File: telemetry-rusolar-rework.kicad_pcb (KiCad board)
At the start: 2 copper layers, 131 parts, among them IC1 TLV62569DBVR, J1 USART Debug, J10 JP, J12 I2C, J13 GR2, J14 GR1, J15 N_GR1, J19 Micro_SD_Card, J2 SPI, J20 USB_C_Receptacle_USB2.0_14P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

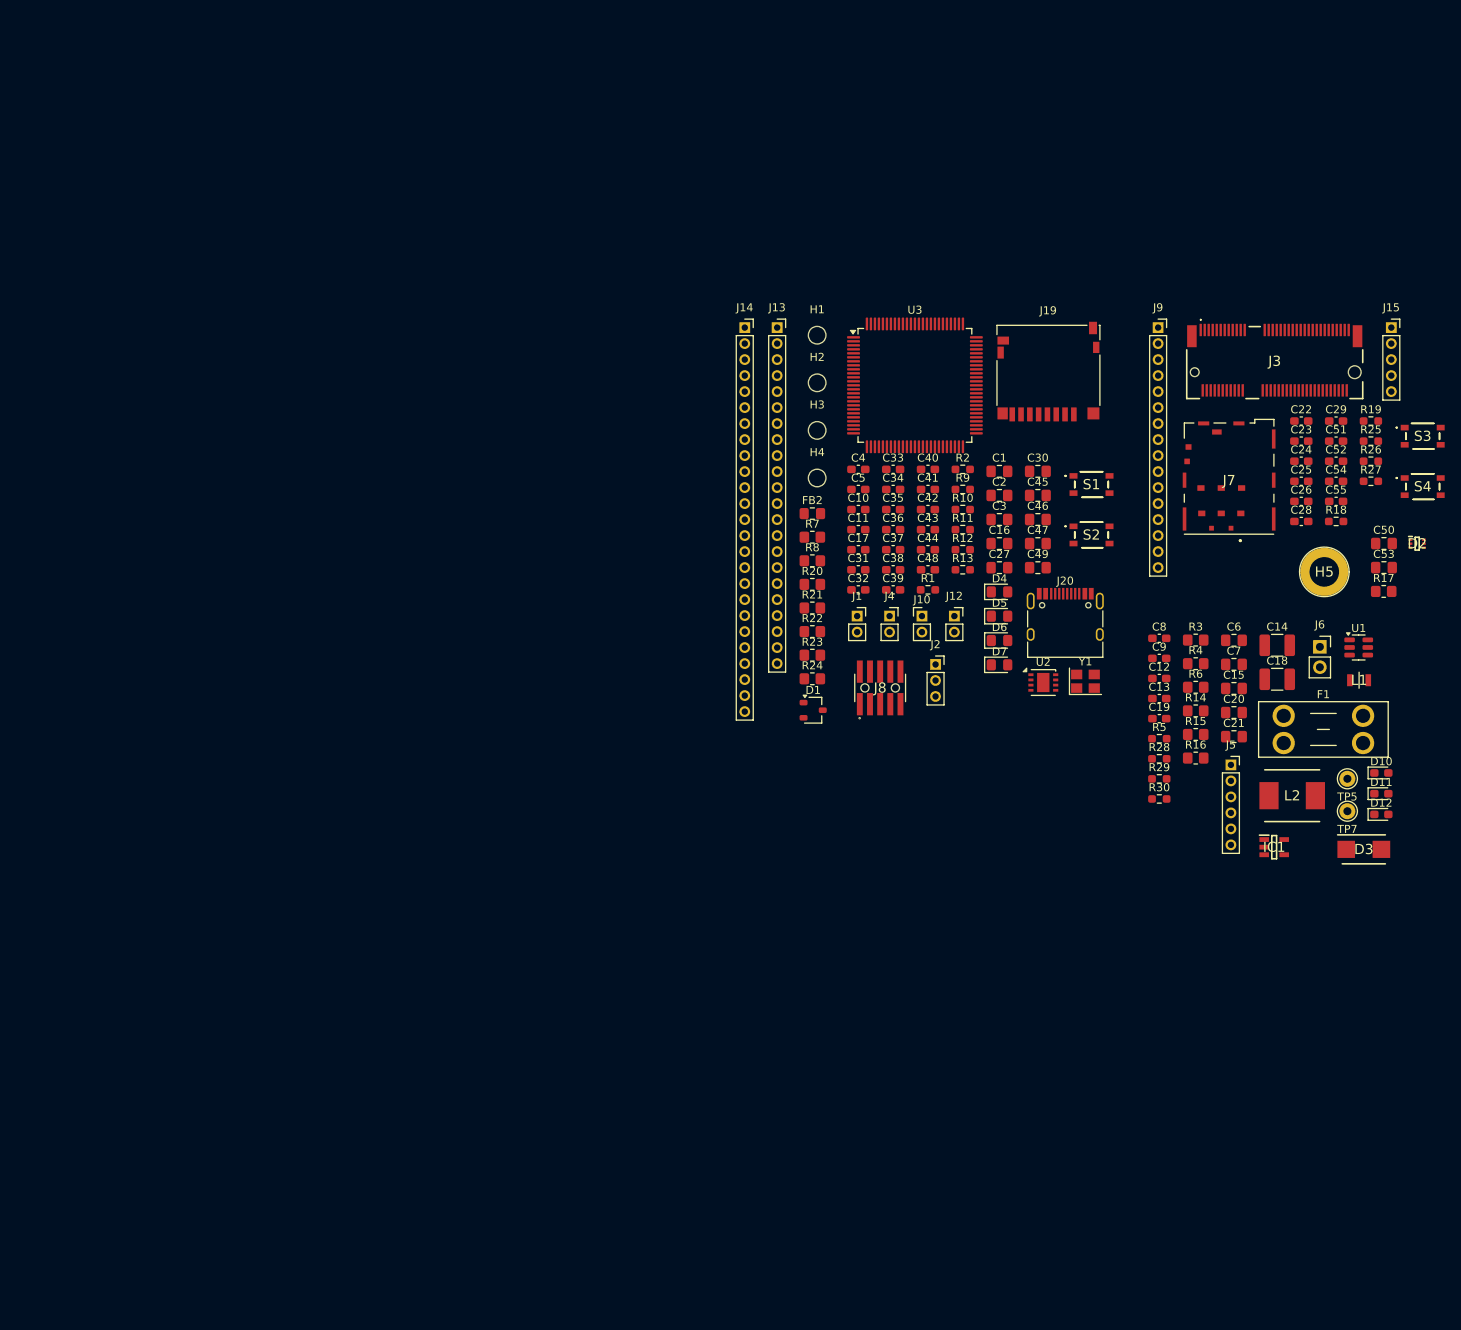
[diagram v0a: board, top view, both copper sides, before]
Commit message: Layout parts
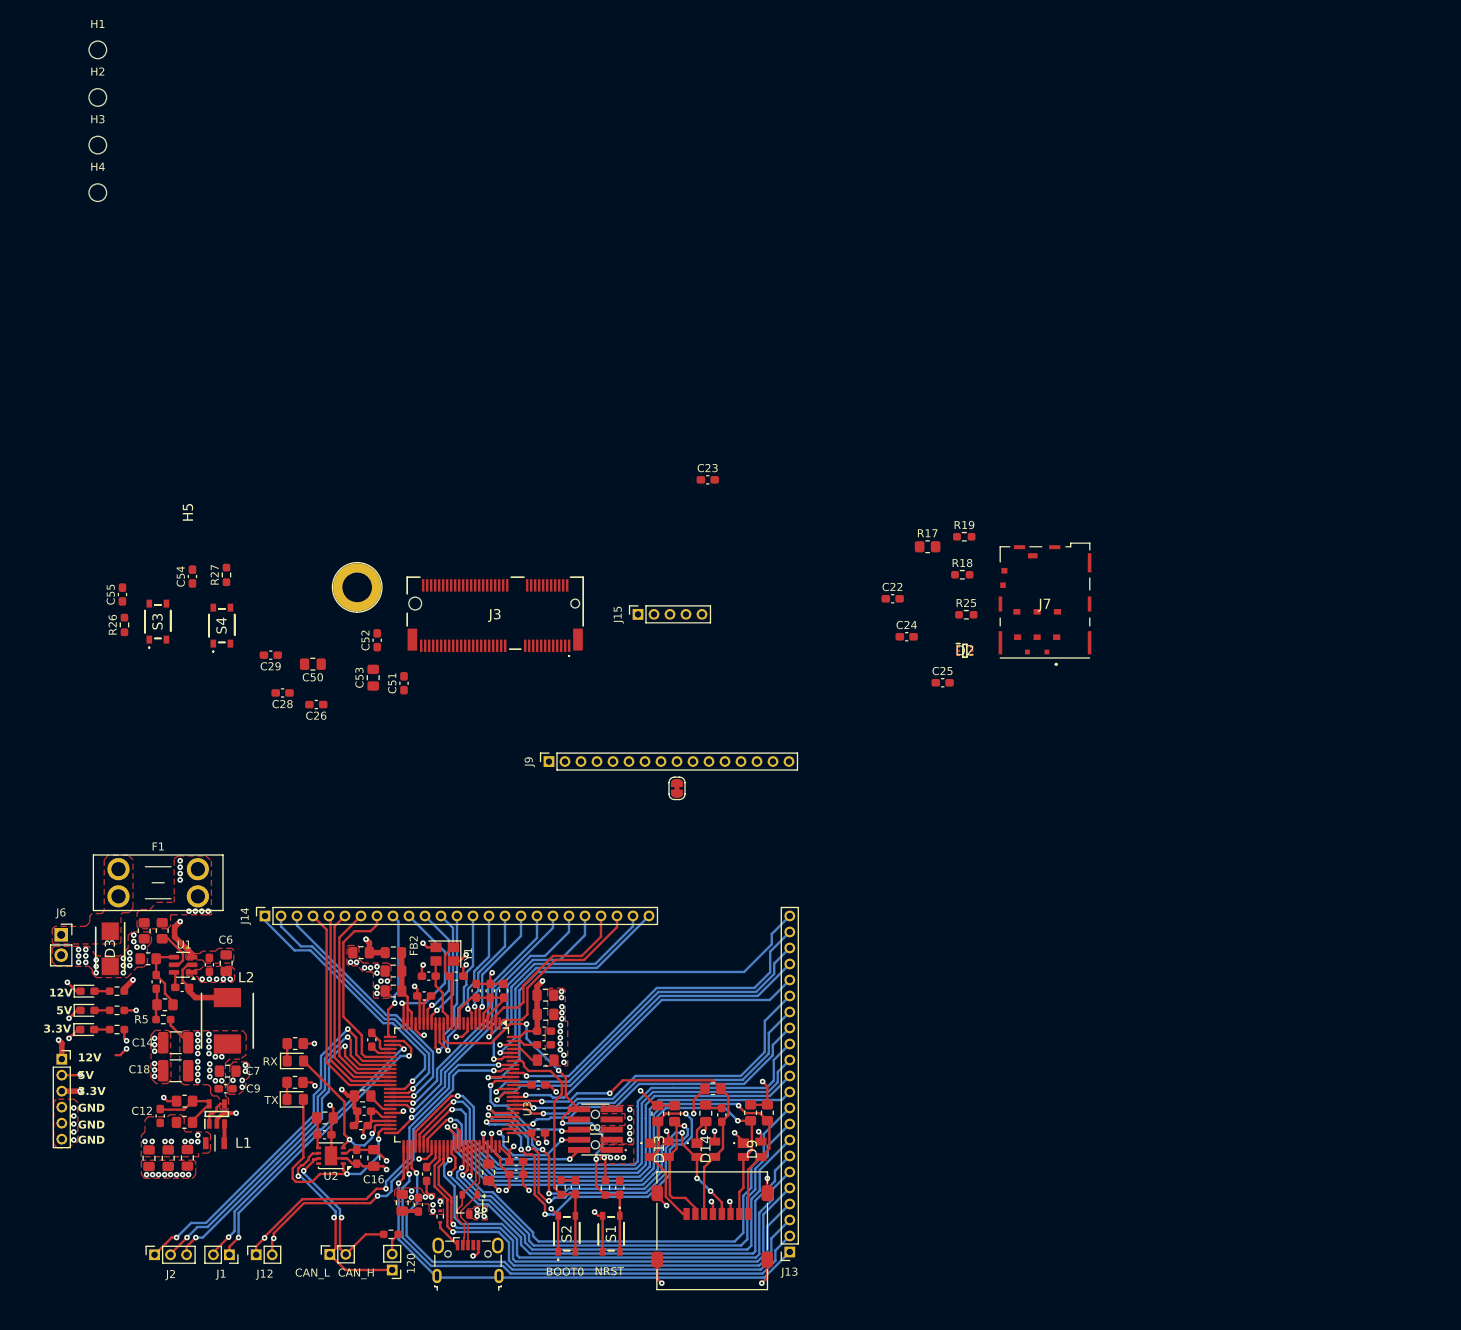
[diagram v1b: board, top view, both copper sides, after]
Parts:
- removed D4: SD-ON, LED_SMD:LED_0805_2012Metric_Pad1.15x1.40mm_HandSolder
- removed D7: PWR, LED_SMD:LED_0805_2012Metric_Pad1.15x1.40mm_HandSolder
- removed J20: USB_C_Receptacle_USB2.0_14P, Connector_USB:USB_C_Receptacle_HRO_TYPE-C-31-M-12
- removed R10, R11: 5k1, Resistor_SMD:R_0603_1608Metric_Pad0.98x0.95mm_HandSolder
- removed R12: 1k5, Resistor_SMD:R_0603_1608Metric_Pad0.98x0.95mm_HandSolder
- removed R9: 330, Resistor_SMD:R_0603_1608Metric_Pad0.98x0.95mm_HandSolder
- removed TP5, TP7: OUT_TP, Connector_Pin:Pin_D1.0mm_L10.0mm
- added C56: 100n, Capacitor_SMD:C_0603_1608Metric_Pad1.08x0.95mm_HandSolder, F.Cu at (70.3, 166.5)
- added C57: 1u, Capacitor_SMD:C_0805_2012Metric_Pad1.18x1.45mm_HandSolder, F.Cu at (68.2, 166.2)
- added C58: 100n, Capacitor_SMD:C_0603_1608Metric_Pad1.08x0.95mm_HandSolder, F.Cu at (58.5, 157.8)
- added C59: 10u, Capacitor_SMD:C_0805_2012Metric_Pad1.18x1.45mm_HandSolder, F.Cu at (58.6, 155.7)
- added D13: LSR05-TP, SamacSys_Parts:LSR05TP, F.Cu at (100.4, 159.6)
- added D14: LSR05-TP, SamacSys_Parts:LSR05TP, F.Cu at (106.2, 159.6)
- added D8: VESD05A1-02VHG3-08, SamacSys_Parts:VESD05A102VHG308, F.Cu at (73.0, 168.0)
- added D9: LSR05-TP, SamacSys_Parts:LSR05TP, F.Cu at (112.0, 159.6)
- added J11: USB_B_Micro, Connector_USB:USB_Micro-B_Wuerth_629105150521, F.Cu at (76.5, 173.4)
- added JP1: SolderJumper, Jumper:SolderJumper-2_P1.3mm_Bridged_RoundedPad1.0x1.5mm, F.Cu at (102.6, 114.5)
- J19: footprint Connector_Card:microSD_HC_Hirose_DM3D-SF -> Connector_Card:microSD_HC_Molex_47219-2001
- moved D10 164.0 mm to (28.9, 139.8)
- moved D12 164.0 mm to (28.9, 144.6)
- moved D11 164.0 mm to (28.9, 142.2)
- moved J6 161.4 mm to (25.6, 132.8)
- moved S3 159.8 mm to (37.7, 93.6), turned to 90 degrees
- moved D3 157.2 mm to (31.8, 134.5), turned to -90 degrees
- moved R26 157.1 mm to (33.5, 94.0), turned to 90 degrees
- moved L1 154.3 mm to (44.9, 158.8), turned to 180 degrees
- moved U1 152.2 mm to (40.9, 136.5), turned to 180 degrees
- moved C55 152.2 mm to (33.3, 90.2), turned to 90 degrees
- moved S4 151.1 mm to (45.7, 94.1), turned to 90 degrees
- moved J5 150.7 mm to (25.7, 148.3)
- moved C15 147.8 mm to (36.6, 160.7), turned to -90 degrees
- moved C14 146.4 mm to (39.9, 146.2), turned to 180 degrees
- moved C18 146.1 mm to (39.9, 149.8), turned to 180 degrees
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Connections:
- C2 pad 2: Net-(C1-Pad2) -> Net-(C2-Pad2)
- C3 pad 2: Net-(C1-Pad2) -> Net-(C3-Pad2)
- D1 pad 1: /USB_D- -> /USB_D+
- D1 pad 2: /USB_D+ -> /USB_D-
- J10 pad 1: /CAN2_RX -> /CAN_N
- J13 pad 1: /PA0 -> /PB15
- J13 pad 10: /PB2 -> /PA10
- J13 pad 11: /PB4 -> /PD13
- J13 pad 12: /PB5 -> /PD12
- J13 pad 13: /PB8 -> /PD11
- J13 pad 14: /PB9 -> /PD10
- J13 pad 15: /PB10 -> /PA15
- J13 pad 16: /PB11 -> /PD0
- J13 pad 17: /PB14 -> /PD1
- J13 pad 18: /PB15 -> /PD3
- J13 pad 19: /PC0 -> /PD4
- J13 pad 2: /PA1 -> /PD8
- J13 pad 20: /PC1 -> /PD5
- J13 pad 21: /PC2_C -> /PB5
- J13 pad 22: /PC3_C -> /PB4
- J13 pad 3: /PA4 -> /PD9
- J13 pad 4: /PA8 -> PD14*
- J13 pad 5: /PA9 -> /PD15
- J13 pad 6: /PA10 -> /PC6
- J13 pad 7: /PA15 -> /PC7
- J13 pad 8: /PB0 -> /PA8
- J13 pad 9: /PB1 -> /PA9
- J14 pad 1: /PC4 -> /PB2
- J14 pad 10: /PE5 -> /PA0
- J14 pad 11: /PE7 -> /PC3_C
- J14 pad 12: /PE8 -> /PC2_C
- J14 pad 13: /PD0 -> /PC1
- J14 pad 14: /PD1 -> /PC0
- J14 pad 15: /PD3 -> /PC15
- J14 pad 16: /PD4 -> /PC14
- J14 pad 17: /PD5 -> /PC13
- J14 pad 18: /PD8 -> /PB10
- J14 pad 19: /PD9 -> /PB11
- J14 pad 2: /PC5 -> /PE7
- J14 pad 20: /PD10 -> /PB14
- J14 pad 21: /PD11 -> /PE5
- J14 pad 22: /PD12 -> /PE4
- J14 pad 23: /PD13 -> /PE2
- J14 pad 24: /PD14 -> /PB8
- J14 pad 25: /PD15 -> /PB9
- J14 pad 3: /PC6 -> /PE8
- J14 pad 4: /PC7 -> /PB1
- J14 pad 5: /PC13 -> /PB0
- J14 pad 6: /PC14 -> /PC5
- J14 pad 7: /PC15 -> /PC4
- J14 pad 8: /PE2 -> /PA4
- J14 pad 9: /PE4 -> /PA1
- J19 pad 4: Net-(J19-VDD) -> +3.3V Buck
- J4 pad 1: Net-(J4-Pin_1) -> /CAN_N
- J4 pad 2: Net-(J4-Pin_2) -> /CAN_P
- R13 pad 2: /CAN2_TX -> /CAN_P
- U2 pad 6: Net-(J4-Pin_1) -> /CAN_N
- U2 pad 7: Net-(J4-Pin_2) -> /CAN_P
- U3 pad 60: /PD14 -> PD14*
- U3 pad 72: Net-(C1-Pad2) -> Net-(C2-Pad2)
- U3 pad 97: Net-(C1-Pad2) -> Net-(C3-Pad2)
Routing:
- net +3.3V Buck: track 0.00 -> 112.4 mm, vias 0 -> 30
- net GND: track 0.00 -> 106.9 mm, vias 0 -> 121
- net /PD10: track 0.00 -> 68.6 mm, vias 0 -> 1
- net /SD1_D1: track 0.00 -> 67.7 mm, vias 0 -> 2
- net /PD11: track 0.00 -> 66.1 mm, vias 0 -> 1
- net /SD1_D0: track 0.00 -> 65.9 mm, vias 0 -> 2
- net /PD9: track 0.00 -> 65.7 mm, vias 0 -> 1
- net /SD1_D2: track 0.00 -> 65.5 mm, vias 0 -> 4
- net /PD8: track 0.00 -> 64.8 mm, vias 0 -> 1
- net /PB15: track 0.00 -> 64.1 mm, vias 0 -> 1
- net /PC6: track 0.00 -> 63.2 mm, vias 0 -> 1
- net /PD12: track 0.00 -> 63.2 mm, vias 0 -> 1
- net /PD15: track 0.00 -> 62.9 mm, vias 0 -> 1
- net PD14*: track 0.00 -> 62.5 mm, vias 0 -> 1
- net /PC7: track 0.00 -> 60.7 mm, vias 0 -> 1
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- added copper zone on F.Cu, net +12V
- added copper zone on In2.Cu, net +12V
- added copper zone on F.Cu, net +12V In
- added copper zone on F.Cu, net +3.3V Buck
- added copper zone on In2.Cu, net +3.3V Buck
- added copper zone on F.Cu, net +5V Buck
- added copper zone on In2.Cu, net +5V Buck
- added copper zone on F.Cu, net GND
- added copper zone on In1.Cu, net GND
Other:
- copper layers 2 -> 4
- board text added: "120"
- board text added: "12V"
- board text added: "3.3V"
- board text added: "5V"
- board text added: "BOOT0"
- board text added: "CAN_H"
- board text added: "CAN_L"
- board text added: "GND"
- board text added: "NRST"
- board text added: "RX"
- board text added: "TX"

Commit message: Layout
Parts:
- JP1: value SolderJumper -> SolderJumper_2_Open; footprint Jumper:SolderJumper-2_P1.3mm_Bridged_RoundedPad1.0x1.5mm -> Jumper:SolderJumper-2_P1.3mm_Open_RoundedPad1.0x1.5mm
- moved H3 169.3 mm to (125.5, 174.0)
- moved H2 146.0 mm to (24.6, 174.0)
- moved H4 112.4 mm to (125.5, 99.5)
- moved S3 79.8 mm to (117.2, 100.1), turned to 180 degrees
- moved C55 79.7 mm to (112.3, 100.0)
- moved H1 77.7 mm to (24.6, 99.6)
- moved R26 77.4 mm to (110.7, 100.0)
- moved C54 72.6 mm to (112.4, 106.0)
- moved S4 72.5 mm to (117.2, 105.9), turned to 180 degrees
- moved R27 66.9 mm to (110.7, 105.9), turned to -90 degrees
- moved C23 54.8 mm to (113.8, 130.2)
- moved R19 51.4 mm to (114.6, 128.4)
- moved R18 51.1 mm to (107.3, 128.4)
- moved R25 48.4 mm to (100.3, 122.0)
- moved R17 48.1 mm to (104.2, 122.0), turned to 180 degrees
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- renumbered F1 to Fuse, J12 to I2C, J1 to USART
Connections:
- J15 pad 2: /blue-note-card/AUX_NCHARGING -> /blue-note-card/CTX
- J15 pad 3: /blue-note-card/VACT_GPS_OUT -> /blue-note-card/RTX
- J15 pad 4: /blue-note-card/VACT_GPS_IN -> unconnected-(J15-Pin_4-Pad4)
- J3 pad 2: GND -> +3.3V Buck
- J3 pad 4: GND -> +3.3V Buck
- J9 pad 10: /blue-note-card/CTX -> /blue-note-card/AUX1
- J9 pad 11: /blue-note-card/RTX -> /blue-note-card/SDA
- J9 pad 12: /blue-note-card/TX -> /blue-note-card/SCL
- J9 pad 13: /blue-note-card/RX -> /blue-note-card/AUX_NCHARGING
- J9 pad 14: /blue-note-card/SCL -> /blue-note-card/VACT_GPS_IN
- J9 pad 15: /blue-note-card/SDA -> /blue-note-card/VACT_GPS_OUT
- J9 pad 2: /blue-note-card/AUX_TX -> /blue-note-card/TX
- J9 pad 3: /blue-note-card/AUX_RX -> /blue-note-card/RX
- J9 pad 4: unconnected-(J9-Pin_4-Pad4) -> /blue-note-card/AUX_TX
- J9 pad 5: /blue-note-card/AUX4 -> /blue-note-card/AUX_RX
- J9 pad 6: /blue-note-card/AUX3 -> /blue-note-card/ATTN
- J9 pad 7: /blue-note-card/AUX2 -> /blue-note-card/AUX4
- J9 pad 8: /blue-note-card/AUX1 -> /blue-note-card/AUX3
- J9 pad 9: /blue-note-card/ATTN -> /blue-note-card/AUX2
- JP1 pad 1: PD14* -> /blue-note-card/VACT_GPS_IN
- JP1 pad 2: /blue-note-card/ATTN -> /blue-note-card/VACT_GPS_OUT
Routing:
- net GND: track 106.9 -> 201.1 mm, vias 121 -> 149
- net /blue-note-card/SIM_VCC: track 0.00 -> 71.7 mm, vias 0 -> 2
- net /blue-note-card/N_NRST: track 0.00 -> 70.2 mm, vias 0 -> 2
- net /blue-note-card/N_BOOT: track 0.00 -> 69.7 mm, vias 0 -> 2
- net /blue-note-card/SIM_RST: track 0.00 -> 63.7 mm
- net /blue-note-card/SIM_NPRESENT: track 0.00 -> 58.5 mm, vias 0 -> 2
- net /blue-note-card/RTX: track 0.00 -> 55.3 mm, vias 0 -> 2
- net /blue-note-card/CTX: track 0.00 -> 53.4 mm, vias 0 -> 2
- net /blue-note-card/SIM_CLK: track 0.00 -> 52.8 mm
- net /blue-note-card/SIM_IO: track 0.00 -> 45.0 mm, vias 0 -> 2
- net /blue-note-card/VACT_GPS_OUT: track 0.00 -> 41.7 mm
- net +3.3V Buck: track 112.4 -> 153.9 mm, vias 30 -> 33
- net /blue-note-card/VACT_GPS_IN: track 0.00 -> 39.7 mm
- net /blue-note-card/AUX_NCHARGING: track 0.00 -> 33.6 mm
- net /blue-note-card/SCL: track 0.00 -> 31.4 mm
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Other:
- board outline added: 108.1 x 81.6 mm
- board text added: "12V IN"
- board text added: "ATTN"
- board text added: "AUX1"
- board text added: "AUX2"
- board text added: "AUX3"
- board text added: "AUX4"
- board text added: "AUX_NCHARGING"
- board text added: "AUX_RX"
- board text added: "AUX_TX"
- board text added: "BlueNoteCard"
- board text added: "CTX"
- board text added: "GPSIN"
- board text added: "GPSOUT"
- board text added: "NOT USED"
- board text added: "N_BOOT"
- board text added: "N_NRST"
- board text added: "Nano Sim"
- board text added: "PA0"
- board text added: "PA1"
- board text added: "PA10"
- board text added: "PA15"
- board text added: "PA4"
- board text added: "PA8"
- board text added: "PA9"
- board text added: "PB0"
- board text added: "PB1"
- board text added: "PB10"
- board text added: "PB11"
- board text added: "PB14"
- board text added: "PB15"
- board text added: "PB2"
- board text added: "PB4"
- board text added: "PB5"
- board text added: "PB8"
- board text added: "PB9"
- board text added: "PC0"
- board text added: "PC1"
- board text added: "PC13"
- board text added: "PC14"
- board text added: "PC15"
- board text added: "PC2"
- board text added: "PC3"
- board text added: "PC4"
- board text added: "PC5"
- board text added: "PC6"
- board text added: "PC7"
- board text added: "PD0"
- board text added: "PD1"
- board text added: "PD10"
- board text added: "PD11"
- board text added: "PD12"
- board text added: "PD13"
- board text added: "PD14*"
- board text added: "PD15"
- board text added: "PD3"
- board text added: "PD4"
- board text added: "PD5"
- board text added: "PD8"
- board text added: "PD9"
- board text added: "PE2"
- board text added: "PE4"
- board text added: "PE5"
- board text added: "PE7"
- board text added: "PE8"
- board text added: "Quang Dinh Bui."
- board text added: "RTX"
- board text added: "RUSolar 26"
- board text added: "Rev 1.0.0 2/12/2025"
- board text added: "SCL"
- board text added: "SD Card"
- board text added: "SDA"
- board text added: "SPI"
- board text added: "Telemetry Mainboard"
- board text added: "USB"
